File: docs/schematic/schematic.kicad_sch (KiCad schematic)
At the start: 24 parts, among them J101 Analog Levers, J12 Button Matrix, J13 Front LED, J5 Motor-PCB, J6 X-Axis, J7 Y-Axis, J8 Z-Axis, Q1 BC548, U1 ProMicroC, U101 74HC4066BQ

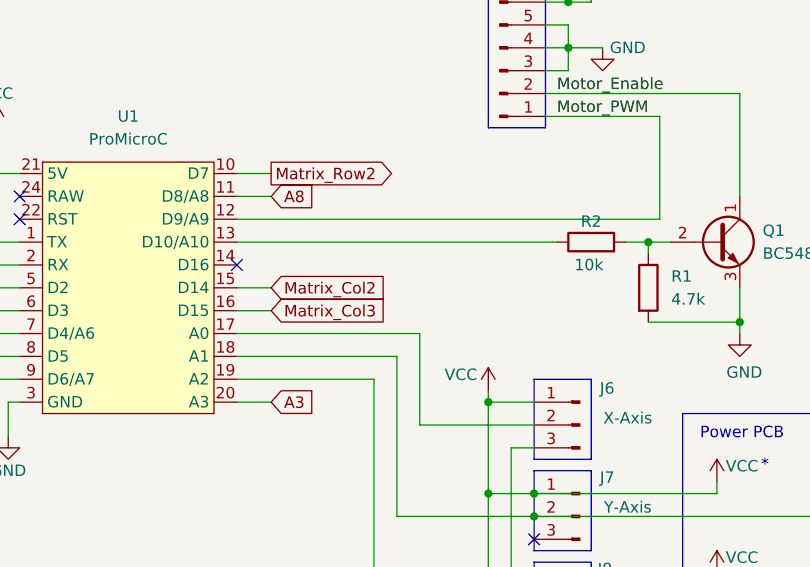
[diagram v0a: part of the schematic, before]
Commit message: add profile switch
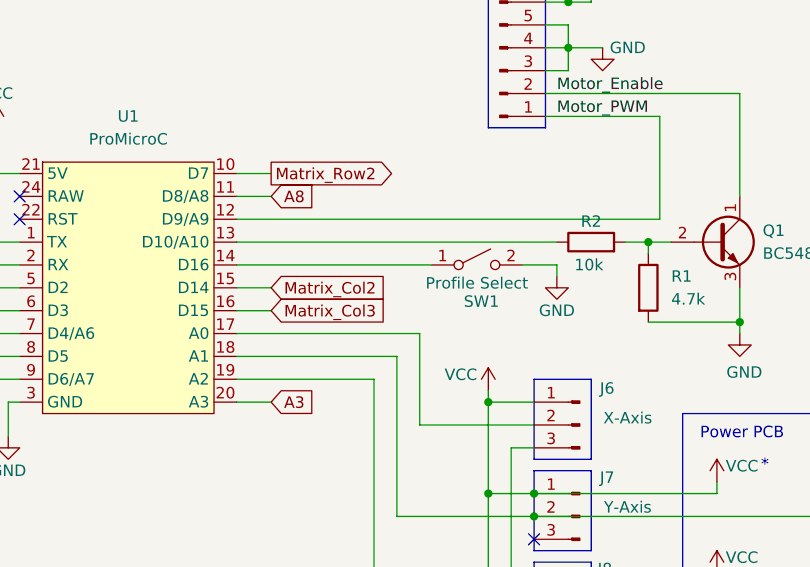
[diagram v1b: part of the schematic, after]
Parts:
- added SW1: Profile Select, symbol Switch:SW_SPST
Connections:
- net GND: now also SW1.2 (B)
- net at U1.14 (D16): now also SW1.1 (A)
- no-connect marks 14 -> 13
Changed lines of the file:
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@@
 	)
 	(no_connect
-		(at 133.35 55.88)
-	)
-	(no_connect
 		(at 109.22 48.26)
 	)
@@
 	(wire
 		(pts
+			(xy 168.91 57.15) (xy 168.91 55.88)
+		)
+		(stroke
+			(width 0)
+			(type default)
+		)
+	)
+	(wire
+		(pts
 			(xy 55.88 55.88) (xy 109.22 55.88)
 		)
@@
 	(wire
 		(pts
+			(xy 133.35 55.88) (xy 154.94 55.88)
+		)
+		(stroke
+			(width 0)
+			(type default)
+		)
+	)
+	(wire
+		(pts
 			(xy 170.18 29.21) (xy 167.64 29.21)
 		)
@@
 	(wire
 		(pts
+			(xy 168.91 55.88) (xy 165.1 55.88)
+		)
+		(stroke
+			(width 0)
+			(type default)
+		)
+	)
+	(wire
+		(pts
 			(xy 166.37 96.52) (xy 163.83 96.52)
 		)
@@
 	)
 	(symbol
+		(lib_id "PCM_SparkFun-PowerSymbol:GND")
+		(at 168.91 57.15 0)
+		(unit 1)
+		(exclude_from_sim no)
+		(in_bom yes)
+		(on_board yes)
+		(dnp no)
+		(fields_autoplaced yes)
+		(property "Reference" "#PWR02"
+			(at 168.91 63.5 0)
+			(effects
+				(font
+					(size 1.27 1.27)
+				)
+				(hide yes)
+			)
+		)
+		(property "Value" "GND"
+			(at 168.91 60.96 0)
+			(do_not_autoplace yes)
+			(effects
+				(font
+					(size 1.27 1.27)
+				)
+			)
+		)
+		(property "Footprint" ""
+			(at 168.91 57.15 0)
+			(effects
+				(font
+					(size 1.27 1.27)
+				)
+				(hide yes)
+			)
+		)
+		(property "Datasheet" ""
+			(at 168.91 57.15 0)
+			(effects
+				(font
+					(size 1.27 1.27)
+				)
+				(hide yes)
+			)
+		)
+		(property "Description" "Power symbol creates a global label with name \"GND\" , ground"
+			(at 168.91 66.04 0)
+			(effects
+				(font
+					(size 1.27 1.27)
+				)
+				(hide yes)
+			)
+		)
+		(pin "1"
+		)
+		(instances
+			(project "schematic"
+				(path "/ebdf8a50-ab25-421e-bb3d-8c800c708f6a"
+					(reference "#PWR02")
+					(unit 1)
+				)
+			)
+		)
+	)
+	(symbol
 		(lib_id "power:PWR_FLAG")
 		(at 250.19 100.33 0)
@@
 					(unit 1)
 				)
+			)
+		)
+	)
+	(symbol
+		(lib_id "Switch:SW_SPST")
+		(at 160.02 55.88 0)
+		(unit 1)
+		(exclude_from_sim no)
+		(in_bom yes)
+		(on_board yes)
+		(dnp no)
+		(property "Reference" "SW1"
+			(at 160.528 59.944 0)
+			(effects
+				(font
+					(size 1.27 1.27)
+				)
+			)
+		)
+		(property "Value" "Profile Select"
+			(at 160.02 57.912 0)
+			(effects
+				(font
+					(size 1.27 1.27)
+				)
+			)
+		)
+		(property "Footprint" ""
+			(at 160.02 55.88 0)
+			(effects
+				(font
+					(size 1.27 1.27)
+				)
+				(hide yes)
+			)
+		)
+		(property "Datasheet" "~"
+			(at 160.02 55.88 0)
+			(effects
+				(font
+					(size 1.27 1.27)
+				)
+				(hide yes)
+			)
+		)
+		(property "Description" "Single Pole Single Throw (SPST) switch"
+			(at 160.02 55.88 0)
+			(effects
+				(font
+					(size 1.27 1.27)
+				)
+				(hide yes)
+			)
+		)
+		(pin "2"
+		)
+		(pin "1"
+		)
+		(instances
+			(project ""
+				(path "/ebdf8a50-ab25-421e-bb3d-8c800c708f6a"
+					(reference "SW1")
+					(unit 1)
+				)
